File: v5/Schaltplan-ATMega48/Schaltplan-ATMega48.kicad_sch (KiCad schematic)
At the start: 6 parts, among them J1 AVR-ISP-6, J3 Conn_01x06_Pin, U1 ATmega48A-P, Y1 Crystal_Small

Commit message: actually do what was written one commit prior
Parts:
- removed J3: Conn_01x06_Pin, Connector_PinSocket_2.54mm:PinSocket_2x03_P2.54mm_Vertical, symbol Connector:Conn_01x06_Pin
- added D10, D11, D2, D3, D4, D5, D6, D7, D8, D9: LED, LED_THT:LED_D3.0mm, symbol Device:LED
- added SW1, SW2, SW3: SW_Push, LED_THT:LED_D3.0mm, symbol Switch:SW_Push
- J1: footprint (none) -> Connector_PinSocket_2.54mm:PinSocket_2x03_P2.54mm_Vertical
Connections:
- net GNDREF: now also D1.1 (K), D10.1 (K), D11.1 (K), D2.1 (K), D3.1 (K), D4.1 (K), D5.1 (K), D6.1 (K), D7.1 (K), D8.1 (K), D9.1 (K), SW1.2, SW2.2, SW3.2
- net at U1.14 (PB0): now also D11.2 (A)
- net at U1.15 (PB1): now also D10.2 (A)
- net at U1.16 (PB2): now also D9.2 (A)
- net at U1.17 (PB3): now also J1.4 (MOSI); no longer J1.3 (SCK)
- net at U1.19 (PB5): now also J1.3 (SCK); no longer J1.4 (MOSI)
- net at U1.2 (PD0): now also D2.2 (A)
- net at U1.23 (PC0): now also D8.2 (A)
- net at U1.24 (PC1): now also D7.2 (A)
- net at U1.25 (PC2): now also D6.2 (A)
- net at U1.26 (PC3): now also D5.2 (A)
- net at U1.27 (PC4): now also D4.2 (A)
- net at U1.28 (PC5): now also D3.2 (A)
- net at U1.3 (PD1): now also D1.2 (A)
- net at U1.4 (PD2): now also SW1.1
- net at U1.5 (PD3): now also SW2.1
- net at U1.6 (PD4): now also SW3.1
- no-connect marks 1 -> 4
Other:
- moved on the sheet: BT1, D1, J1, U1, Y1

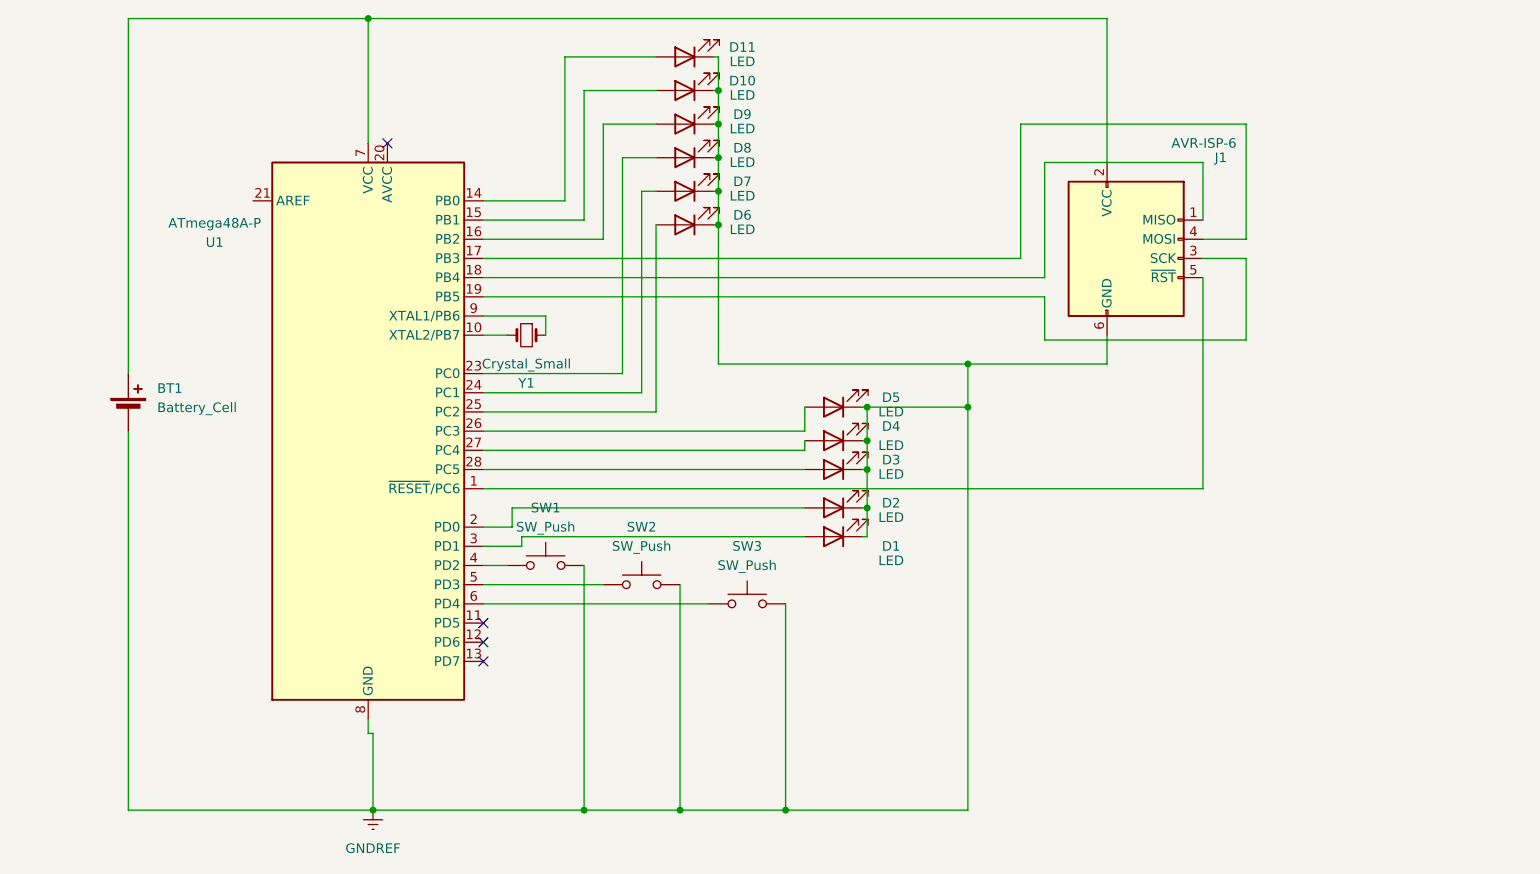
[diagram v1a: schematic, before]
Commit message: Add SRC and DRC for PCB layout, rearrange stuff
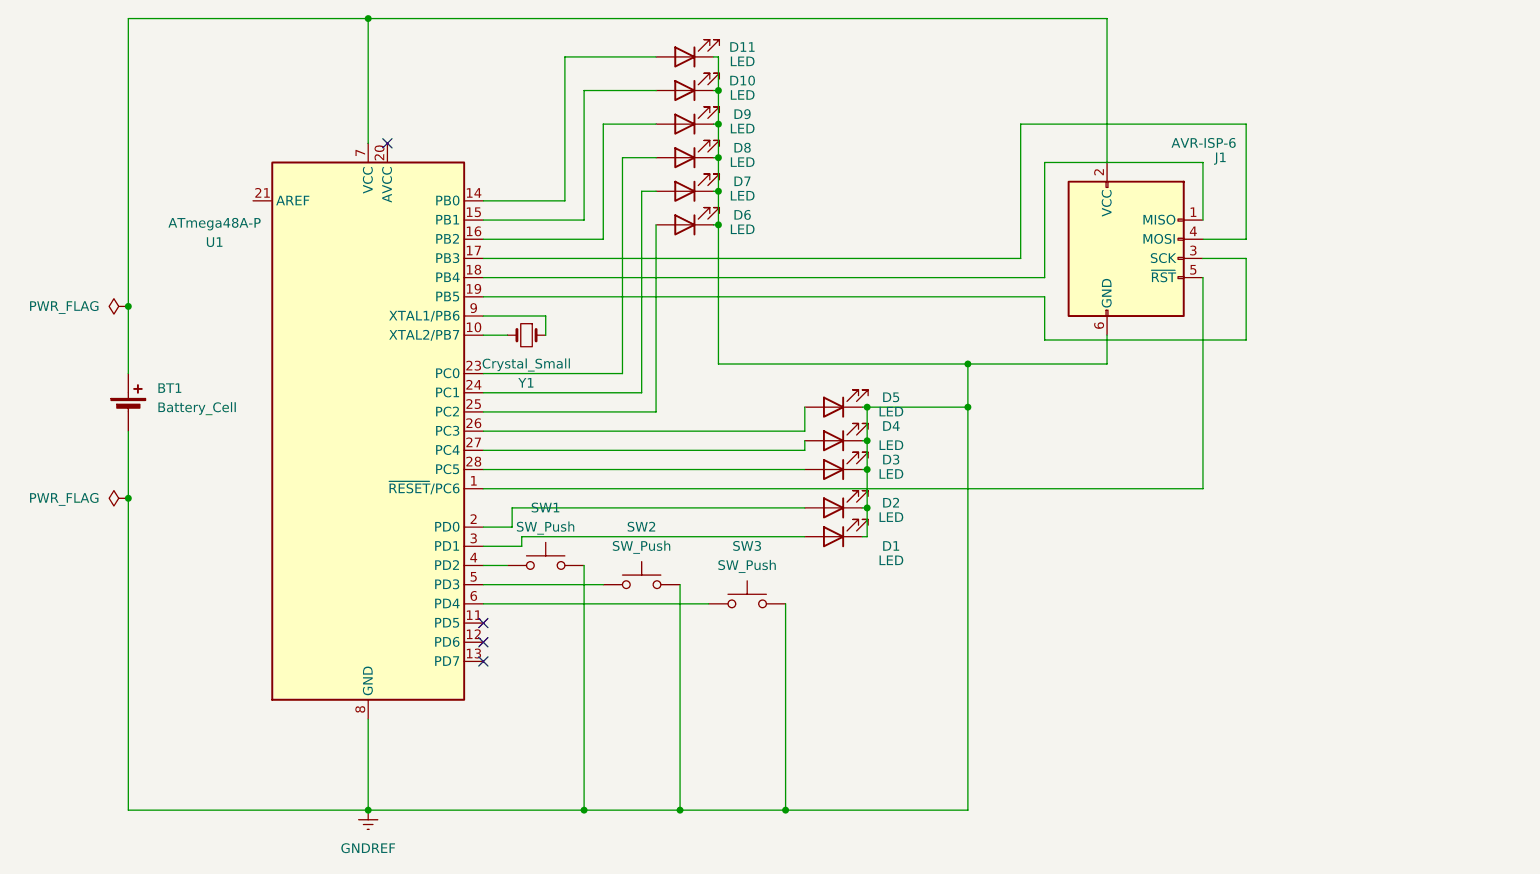
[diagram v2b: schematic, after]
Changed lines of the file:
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@@
 (kicad_sch (version 20230121) (generator eeschema)
   (paper "A4")
+  (junction (at 96.52 150.495) (diameter 0) (color 0 0 0 0)
+  )
   (junction (at 162.56 97.155) (diameter 0) (color 0 0 0 0)
   )
@@
   (junction (at 142.875 73.025) (diameter 0) (color 0 0 0 0)
   )
+  (junction (at 64.77 109.22) (diameter 0) (color 0 0 0 0)
+  )
   (junction (at 96.52 45.72) (diameter 0) (color 0 0 0 0)
   )
@@
   (junction (at 142.875 59.69) (diameter 0) (color 0 0 0 0)
   )
-  (junction (at 97.155 150.495) (diameter 0) (color 0 0 0 0)
+  (junction (at 64.77 83.82) (diameter 0) (color 0 0 0 0)
   )
   (junction (at 175.895 97.155) (diameter 0) (color 0 0 0 0)
@@
     (stroke (width 0) (type default))
   )
-  (wire (pts (xy 64.77 45.72) (xy 64.77 92.71))
+  (wire (pts (xy 64.77 45.72) (xy 64.77 83.82))
     (stroke (width 0) (type default))
   )
@@
     (stroke (width 0) (type default))
   )
-  (wire (pts (xy 97.155 150.495) (xy 125.095 150.495))
+  (wire (pts (xy 64.77 150.495) (xy 96.52 150.495))
     (stroke (width 0) (type default))
   )
@@
     (stroke (width 0) (type default))
   )
-  (wire (pts (xy 64.77 150.495) (xy 97.155 150.495))
+  (wire (pts (xy 64.77 83.82) (xy 64.77 92.71))
     (stroke (width 0) (type default))
   )
@@
     (stroke (width 0) (type default))
   )
-  (wire (pts (xy 96.52 138.43) (xy 96.52 140.335))
+  (wire (pts (xy 96.52 150.495) (xy 125.095 150.495))
     (stroke (width 0) (type default))
   )
@@
     (stroke (width 0) (type default))
   )
+  (wire (pts (xy 64.77 109.22) (xy 64.77 150.495))
+    (stroke (width 0) (type default))
+  )
   (wire (pts (xy 115.57 113.03) (xy 115.57 110.49))
     (stroke (width 0) (type default))
@@
     (stroke (width 0) (type default))
   )
-  (wire (pts (xy 96.52 140.335) (xy 97.155 140.335))
-    (stroke (width 0) (type default))
-  )
   (wire (pts (xy 111.76 74.93) (xy 127.635 74.93))
     (stroke (width 0) (type default))
@@
     (stroke (width 0) (type default))
   )
-  (wire (pts (xy 97.155 140.335) (xy 97.155 150.495))
-    (stroke (width 0) (type default))
-  )
-  (wire (pts (xy 64.77 100.33) (xy 64.77 150.495))
+  (wire (pts (xy 96.52 138.43) (xy 96.52 150.495))
+    (stroke (width 0) (type default))
+  )
+  (wire (pts (xy 64.77 100.33) (xy 64.77 109.22))
     (stroke (width 0) (type default))
   )
@@
     )
   )
-  (symbol (lib_id "power:GNDREF") (at 97.155 150.495 0) (unit 1)
+  (symbol (lib_id "power:GNDREF") (at 96.52 150.495 0) (unit 1)
     (in_bom yes) (on_board yes) (dnp no) (fields_autoplaced)
-    (property "Reference" "#PWR01" (at 97.155 156.845 0)
-      (effects (font (size 1.27 1.27)) hide)
-    )
-    (property "Value" "GNDREF" (at 97.155 155.575 0)
-      (effects (font (size 1.27 1.27)))
-    )
-    (property "Footprint" "" (at 97.155 150.495 0)
-      (effects (font (size 1.27 1.27)) hide)
-    )
-    (property "Datasheet" "" (at 97.155 150.495 0)
+    (property "Reference" "#PWR01" (at 96.52 156.845 0)
+      (effects (font (size 1.27 1.27)) hide)
+    )
+    (property "Value" "GNDREF" (at 96.52 155.575 0)
+      (effects (font (size 1.27 1.27)))
+    )
+    (property "Footprint" "" (at 96.52 150.495 0)
+      (effects (font (size 1.27 1.27)) hide)
+    )
+    (property "Datasheet" "" (at 96.52 150.495 0)
       (effects (font (size 1.27 1.27)) hide)
     )
@@
         (path "/b74f0706-b6d6-4213-a0f9-d18025e70e5a"
           (reference "D11") (unit 1)
+        )
+      )
+    )
+  )
+  (symbol (lib_id "power:PWR_FLAG") (at 64.77 109.22 90) (unit 1)
+    (in_bom yes) (on_board yes) (dnp no) (fields_autoplaced)
+    (property "Reference" "#FLG02" (at 62.865 109.22 0)
+      (effects (font (size 1.27 1.27)) hide)
+    )
+    (property "Value" "PWR_FLAG" (at 60.96 109.22 90)
+      (effects (font (size 1.27 1.27)) (justify left))
+    )
+    (property "Footprint" "" (at 64.77 109.22 0)
+      (effects (font (size 1.27 1.27)) hide)
+    )
+    (property "Datasheet" "~" (at 64.77 109.22 0)
+      (effects (font (size 1.27 1.27)) hide)
+    )
+    (pin "1")
+    (instances
+      (project "Schaltplan-ATMega48"
+        (path "/b74f0706-b6d6-4213-a0f9-d18025e70e5a"
+          (reference "#FLG02") (unit 1)
         )
       )
@@
         )
       )
+    )
+  )
+  (symbol (lib_id "power:PWR_FLAG") (at 64.77 83.82 90) (unit 1)
+    (in_bom yes) (on_board yes) (dnp no) (fields_autoplaced)
+    (property "Reference" "#FLG01" (at 62.865 83.82 0)
+      (effects (font (size 1.27 1.27)) hide)
+    )
+    (property "Value" "PWR_FLAG" (at 60.96 83.82 90)
+      (effects (font (size 1.27 1.27)) (justify left))
+    )
+    (property "Footprint" "" (at 64.77 83.82 0)
+      (effects (font (size 1.27 1.27)) hide)
+    )
+    (property "Datasheet" "~" (at 64.77 83.82 0)
+      (effects (font (size 1.27 1.27)) hide)
+    )
+    (pin "1")
+    (instances
+      (project "Schaltplan-ATMega48"
+        (path "/b74f0706-b6d6-4213-a0f9-d18025e70e5a"
+          (reference "#FLG01") (unit 1)
+        )
+      )

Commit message: first finalization of Platine, DRC errors yet to be fixed
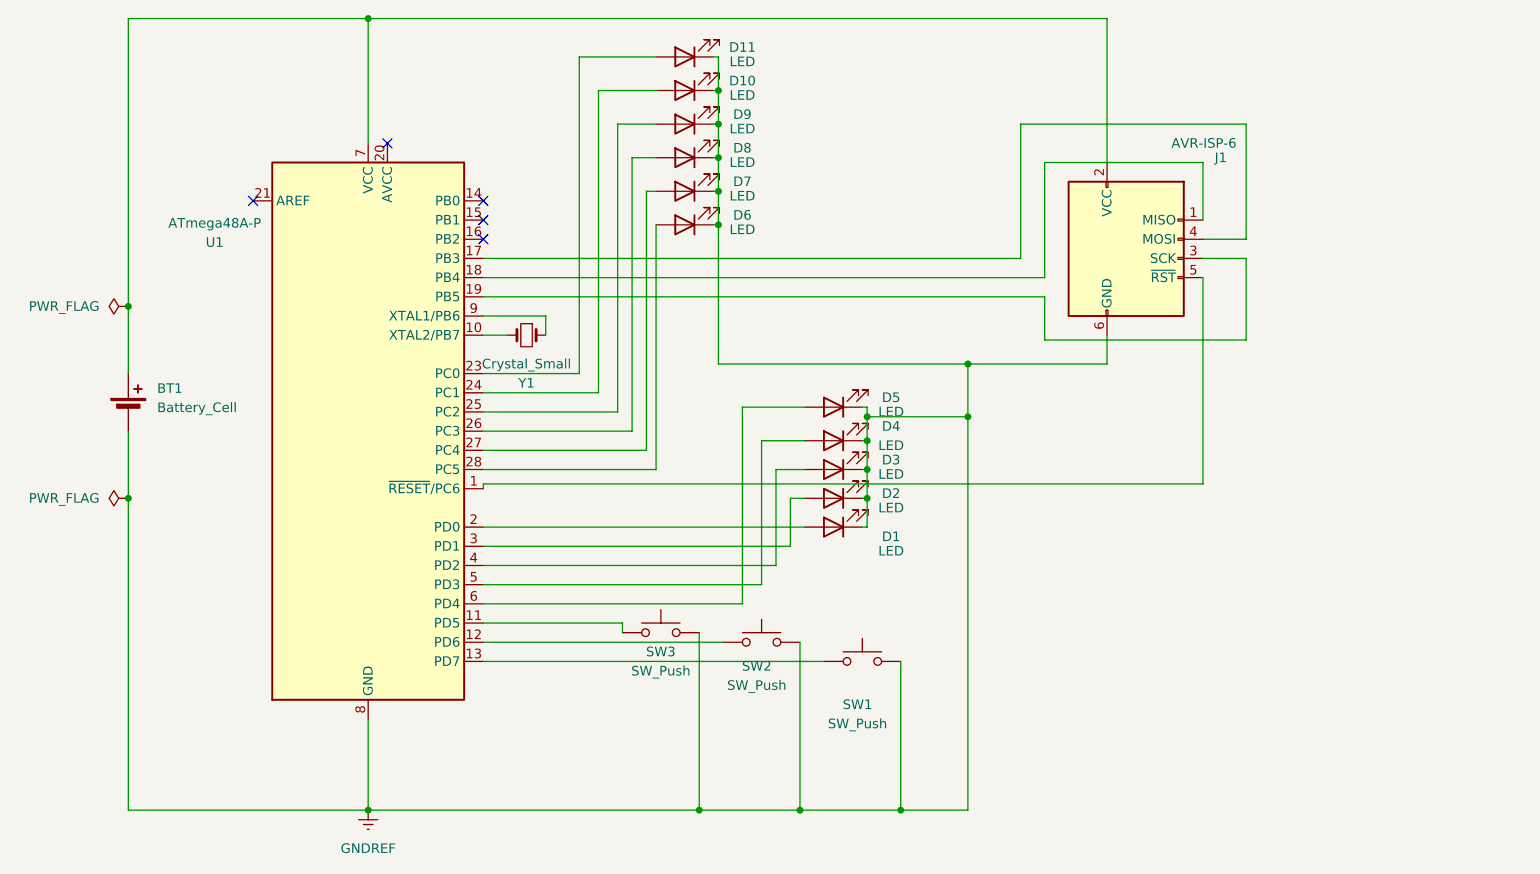
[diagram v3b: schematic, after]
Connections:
- net at D3.2 (A): now also U1.4 (PD2); no longer U1.28 (PC5)
- net at U1.11 (PD5): now also SW3.1
- net at U1.12 (PD6): now also SW2.1
- net at U1.13 (PD7): now also SW1.1
- net at U1.14 (PB0): no longer D11.2 (A)
- net at U1.15 (PB1): no longer D10.2 (A)
- net at U1.16 (PB2): no longer D9.2 (A)
- net at U1.2 (PD0): now also D1.2 (A); no longer D2.2 (A)
- net at U1.23 (PC0): now also D11.2 (A); no longer D8.2 (A)
- net at U1.24 (PC1): now also D10.2 (A); no longer D7.2 (A)
- net at U1.25 (PC2): now also D9.2 (A); no longer D6.2 (A)
- net at U1.26 (PC3): now also D8.2 (A); no longer D5.2 (A)
- net at U1.27 (PC4): now also D7.2 (A); no longer D4.2 (A)
- net at U1.3 (PD1): now also D2.2 (A); no longer D1.2 (A)
- net at U1.5 (PD3): now also D4.2 (A); no longer SW2.1
- net at U1.6 (PD4): now also D5.2 (A); no longer SW3.1
- new net: D6.2 (A), U1.28 (PC5)
- no-connect marks 4 -> 5
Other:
- moved on the sheet: D1, D2, SW1, SW2, SW3
